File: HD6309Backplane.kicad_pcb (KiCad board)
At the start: 2 copper layers, 120.9 x 203.5 mm, 8 parts, among them J1 Conn_01x02_Female, J2 Conn_02x30_Odd_Even, J3 Conn_01x02_Female, J4 Conn_01x02_Female, J5 Conn_01x02_Female, J6 Conn_02x30_Odd_Even, J7 Conn_02x30_Odd_Even, J8 Conn_02x30_Odd_Even

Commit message: align to new expansion position
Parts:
- added J10: Power probe, Connector_PinSocket_2.54mm:PinSocket_1x02_P2.54mm_Vertical, F.Cu at (156.0, 35.4)
- added J9: External power, Connector_PinSocket_2.54mm:PinSocket_1x02_P2.54mm_Vertical, F.Cu at (45.3, 35.5)
- moved J2 1.13 mm to (145.3, 123.3)
- moved J6 0.91 mm to (145.3, 224.6)
- moved J4 0.23 mm to (146.8, 136.9)
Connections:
- J2 pad 45: unconnected-(J2-Pad45) -> Q8
- J6 pad 45: unconnected-(J6-Pad45) -> Q8
- J7 pad 45: unconnected-(J7-Pad45) -> Q8
- J8 pad 45: unconnected-(J8-Pad45) -> Q8
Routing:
- net Q8: track 0.00 -> 256.6 mm, vias 0 -> 2
- net +5V: track 444.2 -> 542.5 mm
- net A9: track 310.6 -> 259.8 mm
- net D4: track 302.1 -> 270.8 mm, vias 0 -> 1
- net ROM/~{RAM}: track 254.1 -> 281.3 mm, vias 2 -> 0
- net GND: track 449.3 -> 474.8 mm
- net Q1: track 251.2 -> 276.1 mm, vias 1 -> 0
- net A15: track 262.9 -> 241.9 mm, vias 1 -> 0
- net D7: track 279.0 -> 260.9 mm, vias 0 -> 1
- net A3: track 291.7 -> 309.1 mm, vias 1 -> 2
- net ~{RESET}: track 252.8 -> 239.5 mm, vias 2 -> 0
- net A1: track 293.7 -> 282.3 mm
- net Clock3: track 308.6 -> 298.2 mm
- net A8: track 259.7 -> 267.6 mm
- net Q6: track 245.9 -> 238.2 mm, vias 0 -> 2
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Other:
- board text added: "HD6309 SBC Expansion Backplane"

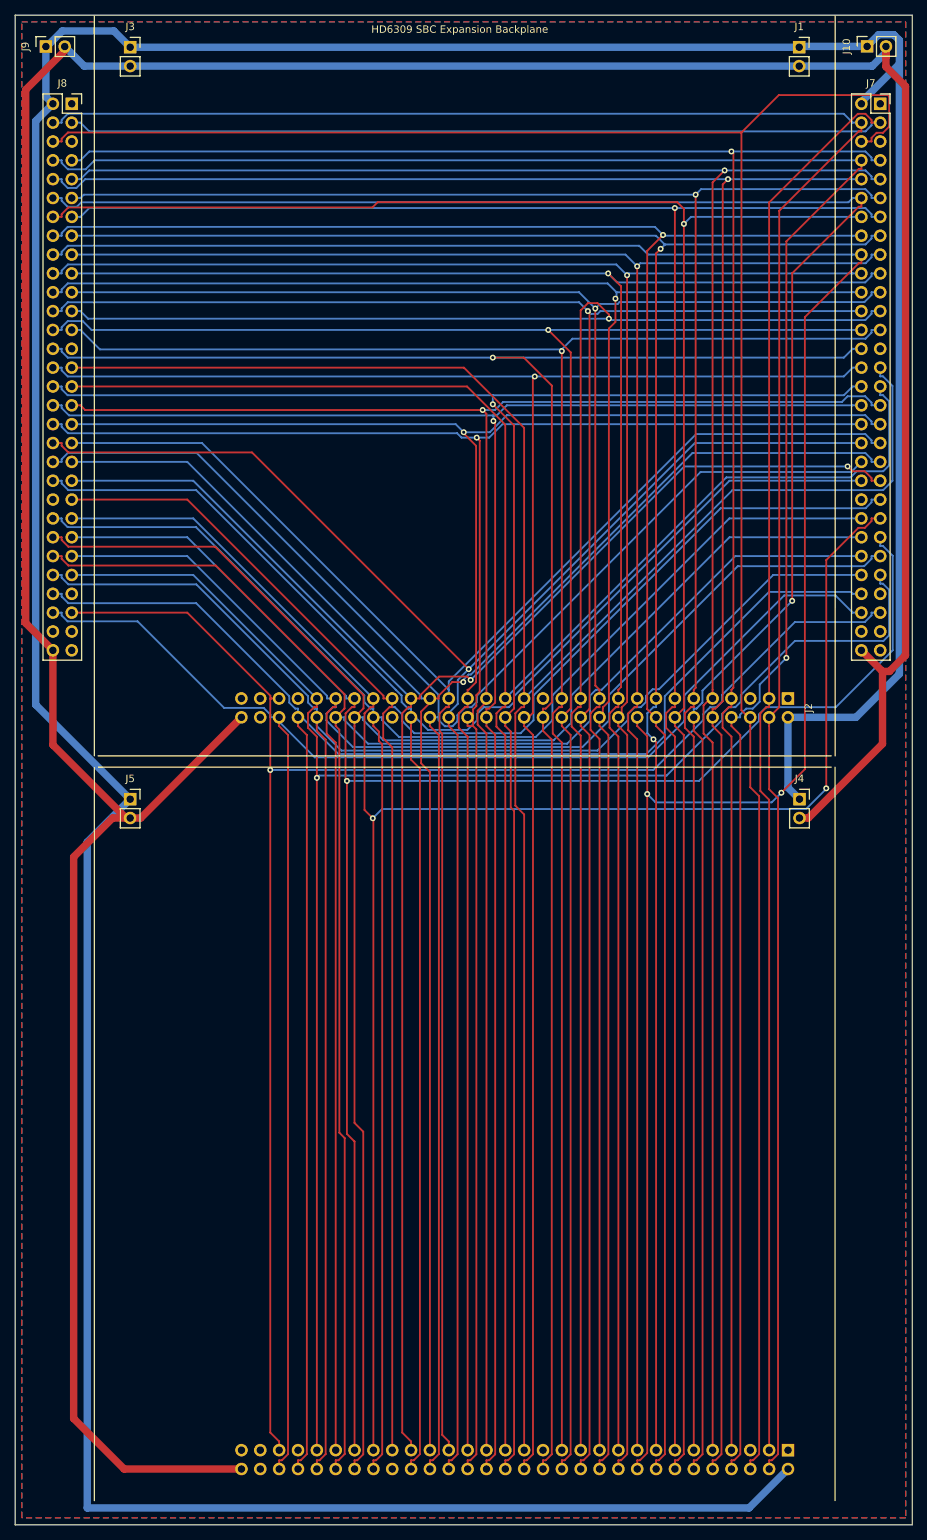
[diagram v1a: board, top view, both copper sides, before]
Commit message: add mapped memory lane
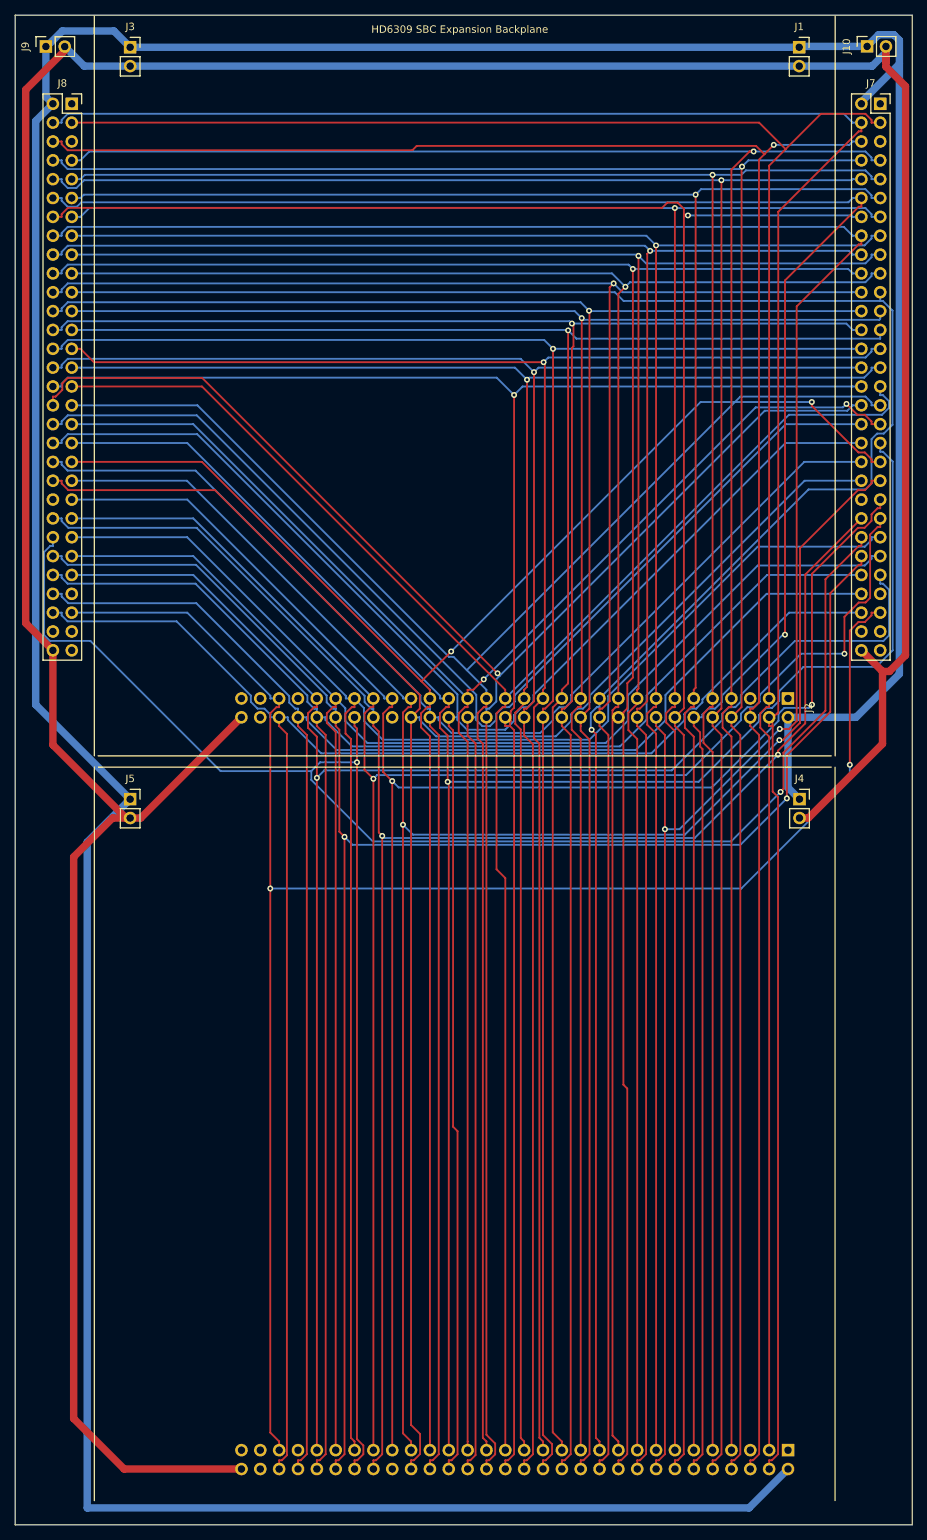
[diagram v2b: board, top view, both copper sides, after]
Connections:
- J2 pad 27: unconnected-(J2-Pad27) -> MAPPED_MEM
- J6 pad 27: unconnected-(J6-Pad27) -> MAPPED_MEM
- J7 pad 27: unconnected-(J7-Pad27) -> MAPPED_MEM
- J8 pad 27: unconnected-(J8-Pad27) -> MAPPED_MEM
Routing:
- net MAPPED_MEM: track 0.00 -> 258.5 mm, vias 0 -> 1
- net ~{NMI}: track 240.2 -> 276.3 mm, vias 0 -> 2
- net A3: track 309.1 -> 276.5 mm, vias 2 -> 1
- net A2: track 279.2 -> 305.7 mm, vias 1 -> 2
- net Q1: track 276.1 -> 250.6 mm
- net ROM/~{RAM}: track 281.3 -> 255.9 mm, vias 0 -> 1
- net Q4: track 242.1 -> 265.2 mm, vias 0 -> 1
- net D5: track 266.3 -> 289.0 mm
- net Q6: track 238.2 -> 259.1 mm
- net MRDY: track 227.0 -> 245.1 mm, vias 1 -> 2
- net Clock6: track 306.6 -> 290.5 mm, vias 0 -> 1
- net ~{RESET}: track 239.5 -> 252.8 mm, vias 0 -> 2
- net ~{FIRQ}: track 238.4 -> 250.7 mm, vias 0 -> 2
- net Q8: track 256.6 -> 245.7 mm
- net Q7: track 241.2 -> 251.3 mm, vias 0 -> 2
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- removed copper zone on B.Cu, net GND
- removed copper zone on F.Cu, net GND
